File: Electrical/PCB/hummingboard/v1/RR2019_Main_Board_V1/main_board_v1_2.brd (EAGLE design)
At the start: 100 x 75 mm, 144 parts, among them CN1 MIRCO_B, IC1 OR_SC70-5, J10 I2C_5V_4, J11 SERVO_LEFT, J12 SERVO_RIGHT, J13 ESC, J14 5V_INPUT, J15 QUAD_ENCODER_2, J16 7.2V_INPUT, J17 I2C_5V_FXIO_1, J18 I2C_5V_FXIO_2, J19 JETSON_TRIGGER, J2 REAR_ENCODER, J20 QUAD_ENCODER_1, J21 BLDC_HALL, J22 SPI_FXIO_1, J3 FRONT_ENCODER, J4 I2C_1V8_1, J5 SPI_2, J6 WIRELESS_MODULE, J7 UART_0, J8 UART_2, J9 STEERING_ANGLE, Q1 BSS138, Q3 DMP2066LSN, Q4 BSS138, Q5 BSS138, Q6 BSS138, Q7 BSS138, Q8 BSS138, U3 ICM-20948, U4 PCA9306

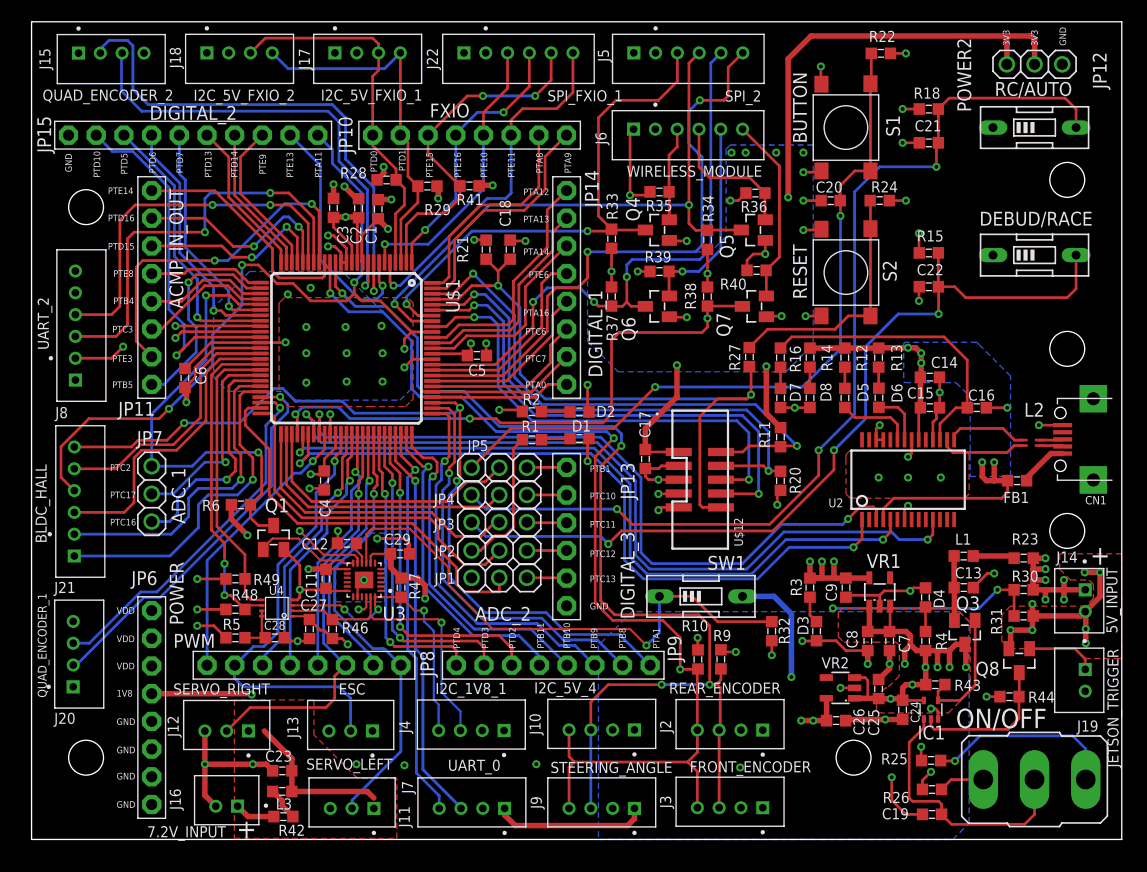
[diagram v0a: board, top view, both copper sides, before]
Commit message: increase 7.2V power plane size
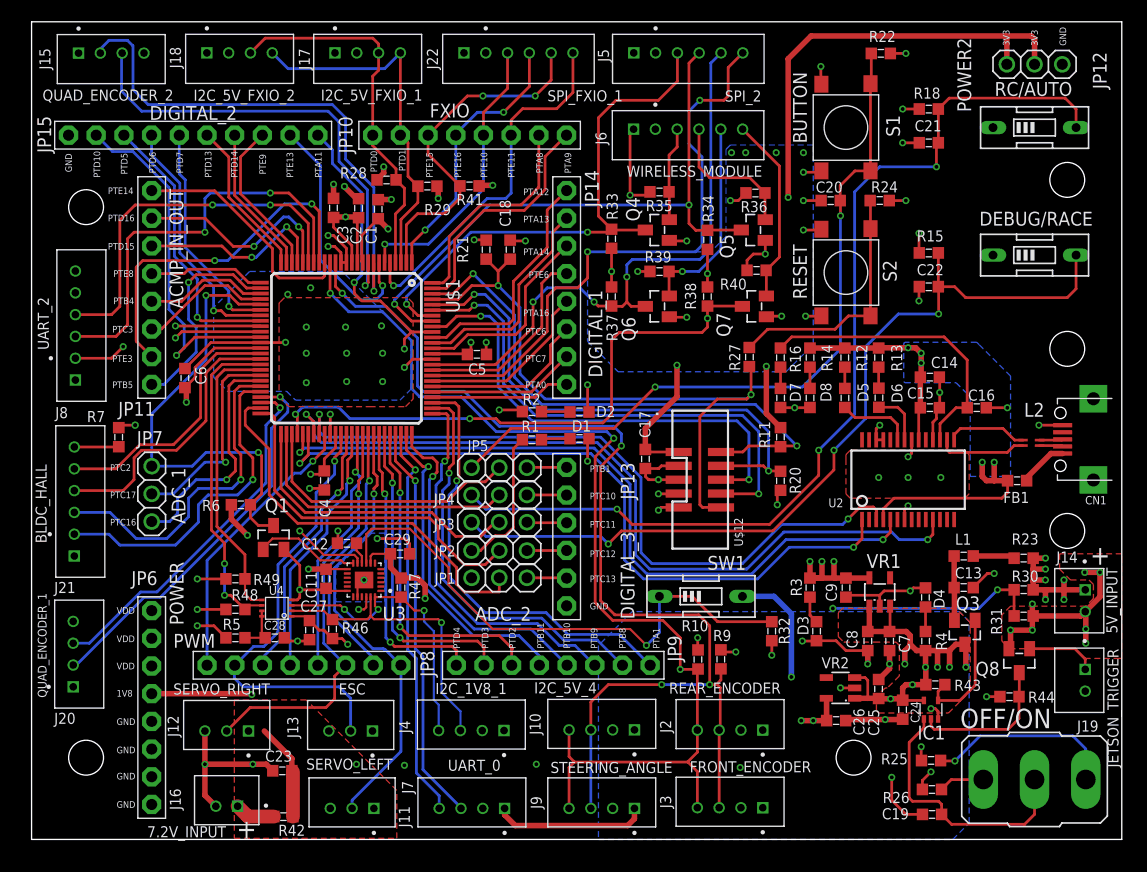
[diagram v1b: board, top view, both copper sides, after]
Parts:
- removed L3: TBD, RobotRacing2019_Master:0603SMT
- added R7: TBD, RobotRacing2019_Master:0603SMT
- S3: value ON/OFF -> OFF/ON
- moved C27 0.10 mm to (25.5, 19.2)
- moved C5 0.10 mm to (40.9, 44.5)
- renumbered DEBUD/RACE to DEBUG/RACE
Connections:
- removed net N$36: L3.1, R42.1
- new net N$4: J21.6, R7.1
- net +7.2V: now also R42.1; no longer L3.2
- net +VDD: now also R7.2
- net ADC0_SE1_/_ACMP0_IN1_/_FTM1_CH1: no longer J21.6
- net FTM1_CH2_/_ADC0_SE12: now also J21.2; no longer J21.1
- net FTM1_CH3_/_ADC0_SE13: now also J21.3; no longer J21.2
- net FTM1_CH6_/_ADC0_SE8: now also J21.4; no longer J21.3
- net GND: now also J21.1
- net PTA11_/_FTM1_CH5: no longer J21.4
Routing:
- net PTA11_/_FTM1_CH5: track 70.7 -> 26.9 mm, vias 4 -> 2
- net ADC0_SE1_/_ACMP0_IN1_/_FTM1_CH1: track 79.2 -> 40.4 mm, vias 3 -> 1
- net +7.2V: track 14.4 -> 8.80 mm
- net N$4: track 0.00 -> 4.09 mm
- net N$36: track 3.07 -> 0.00 mm
- net FTM1_CH6_/_ADC0_SE8: track 27.9 -> 25.8 mm
- net +VDD: track 153.9 -> 155.5 mm, vias 35 -> 36
- net FTM1_CH3_/_ADC0_SE13: track 29.3 -> 30.5 mm

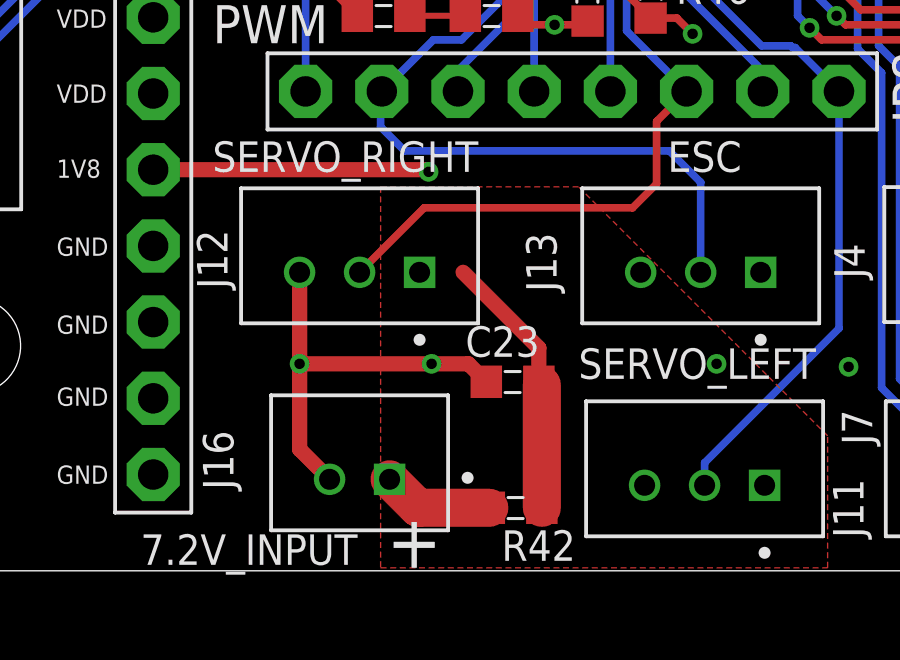
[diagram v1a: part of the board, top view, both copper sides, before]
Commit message: remove inductor from 7.2V input / modify GND plane
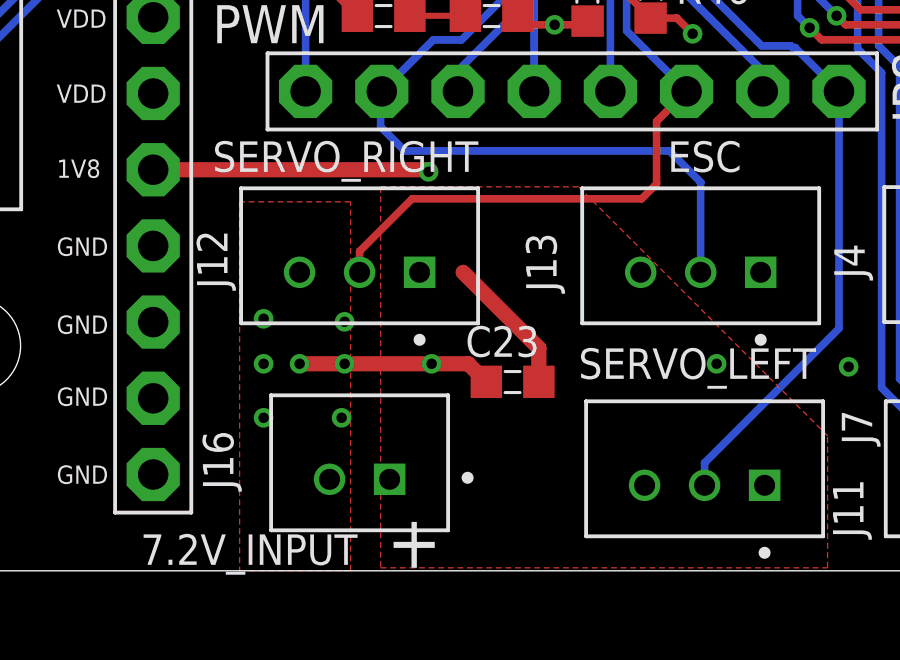
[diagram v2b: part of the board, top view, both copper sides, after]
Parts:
- removed R42: TBD, RobotRacing2019_Master:0603SMT
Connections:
- removed net N$34: J16.1, R42.2
- net +7.2V: now also J16.1; no longer R42.1
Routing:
- net GND: track 178.8 -> 171.5 mm, vias 74 -> 80
- net +7.2V: track 8.80 -> 4.70 mm
- net N$34: track 3.72 -> 0.00 mm
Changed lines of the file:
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@@
 <drawing>
 <settings>
-<setting alwaysvectorfont="yes"/>
+<setting alwaysvectorfont="no"/>
 <setting verticaltext="up"/>
 </settings>
@@
 <attribute name="NAME" x="23.9" y="8.15" size="1.016" layer="25" rot="R180"/>
 </element>
-<element name="R42" library="RobotRacing2019_Master" package="0603SMT" value="TBD" x="23.1" y="2.1" smashed="yes" rot="R180">
-<attribute name="NAME" x="25.1" y="1.35" size="1.016" layer="25" rot="R180"/>
-</element>
 <element name="J19" library="RobotRacing2019_Master" package="JST_B2B-PH-K-S(LF)(SN)" value="JETSON_TRIGGER" x="96.1" y="14.6" smashed="yes" rot="R90">
 <attribute name="NAME" x="95.89608125" y="9.89518125" size="1.01753125" layer="25"/>
@@
 <via x="20.3" y="6.9" extent="1-16" drill="0.35"/>
 <via x="15.9" y="6.9" extent="1-16" drill="0.35"/>
-<wire x1="15.9" y1="6.9" x2="15.9" y2="9.95" width="0.508" layer="1"/>
-<wire x1="16.9" y1="3.05" x2="15.9" y2="4.05" width="0.508" layer="1"/>
-<wire x1="15.9" y1="4.05" x2="15.9" y2="6.9" width="0.508" layer="1"/>
 <wire x1="15.9" y1="6.9" x2="20.3" y2="6.9" width="0.508" layer="1"/>
 <wire x1="20.3" y1="6.9" x2="21.525" y2="6.9" width="0.508" layer="1"/>
@@
 </polygon>
 <contactref element="J21" pad="1"/>
+<via x="14.7" y="6.9" extent="1-16" drill="0.35"/>
+<via x="17.4" y="8.3" extent="1-16" drill="0.35"/>
+<via x="17.4" y="6.9" extent="1-16" drill="0.35"/>
+<via x="17.3" y="5.1" extent="1-16" drill="0.35"/>
+<via x="14.7" y="8.4" extent="1-16" drill="0.35"/>
+<via x="14.7" y="5.1" extent="1-16" drill="0.35"/>
+<polygon width="0.4064" layer="1">
+<vertex x="13.9" y="12.3"/>
+<vertex x="13.9" y="0"/>
+<vertex x="17.4" y="0"/>
+<vertex x="17.6" y="0"/>
+<vertex x="17.6" y="12.2"/>
+<vertex x="17.6" y="12.3"/>
+</polygon>
 </signal>
 <signal name="+VDD">
@@
 <contactref element="J12" pad="2"/>
 <contactref element="JP8" pad="3"/>
-<wire x1="17.9" y1="9.95" x2="20.05" y2="12.1" width="0.254" layer="1"/>
+<wire x1="19.65" y1="12.4" x2="17.9" y2="10.65" width="0.254" layer="1"/>
+<wire x1="17.9" y1="9.95" x2="17.9" y2="10.65" width="0.254" layer="1"/>
 <wire x1="27.8" y1="14.98" x2="28.8" y2="15.98" width="0.254" layer="1"/>
 <wire x1="27.8" y1="14.98" x2="27.8" y2="12.9" width="0.254" layer="1"/>
-<wire x1="20.05" y1="12.1" x2="27" y2="12.1" width="0.254" layer="1"/>
-<wire x1="27" y1="12.1" x2="27.8" y2="12.9" width="0.254" layer="1"/>
+<wire x1="19.65" y1="12.4" x2="27.3" y2="12.4" width="0.254" layer="1"/>
+<wire x1="27.3" y1="12.4" x2="27.8" y2="12.9" width="0.254" layer="1"/>
 <via x="30" y="31.7" extent="1-16" drill="0.35"/>
 <wire x1="30" y1="31.7" x2="30" y2="28.6" width="0.254" layer="16"/>
@@
 <contactref element="J11" pad="1"/>
 <contactref element="J12" pad="1"/>
-<polygon width="0.508" layer="1" rank="2">
+<polygon width="0.8128" layer="1" rank="2">
 <vertex x="18.6" y="12.8"/>
 <vertex x="18.6" y="0.1"/>
@@
 <vertex x="25.2" y="12.8"/>
 </polygon>
-<contactref element="R42" pad="1"/>
-<wire x1="23.975" y1="2.1" x2="23.975" y2="6.2" width="1.27" layer="1"/>
-</signal>
-<signal name="N$34">
 <contactref element="J16" pad="1"/>
-<contactref element="R42" pad="2"/>
-<wire x1="18.9" y1="3.05" x2="19.85" y2="2.1" width="1.27" layer="1"/>
-<wire x1="19.85" y1="2.1" x2="22.225" y2="2.1" width="1.27" layer="1"/>
 </signal>
 <signal name="N$39">

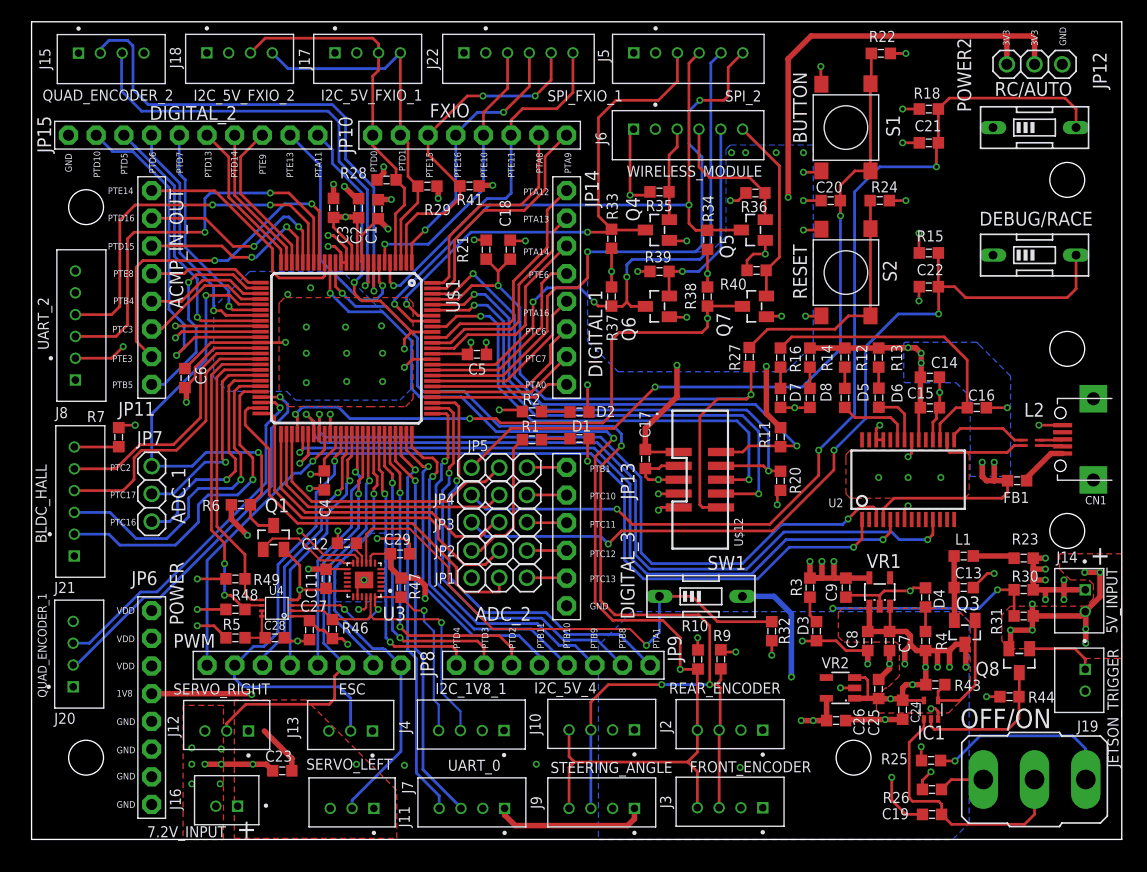
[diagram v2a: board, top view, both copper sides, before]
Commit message: add extra GND plane and via
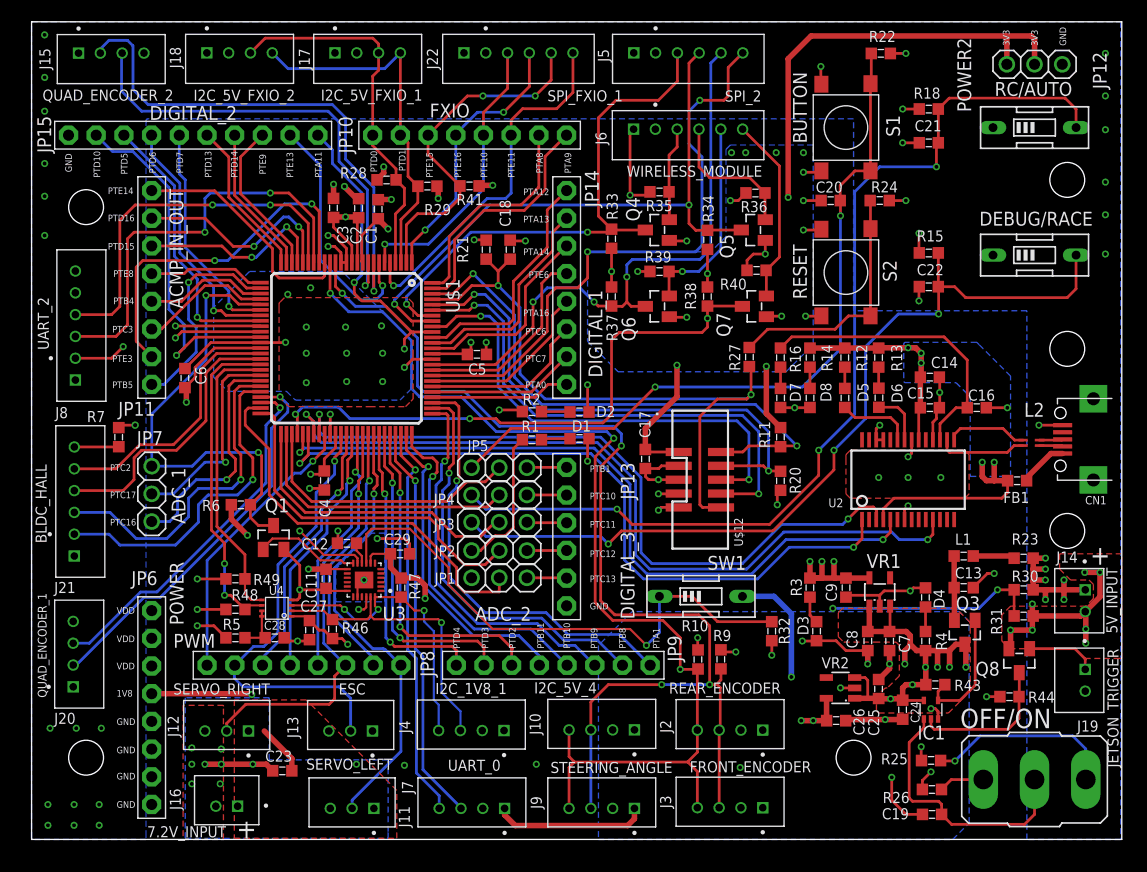
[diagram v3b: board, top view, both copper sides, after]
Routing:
- net GND: vias 80 -> 101
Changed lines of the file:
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@@
 <drawing>
 <settings>
-<setting alwaysvectorfont="no"/>
+<setting alwaysvectorfont="yes"/>
 <setting verticaltext="up"/>
 </settings>
@@
 <vertex x="100" y="75"/>
 </polygon>
-<polygon width="0.254" layer="2">
+<polygon width="0.508" layer="2">
 <vertex x="14.1" y="0.1"/>
 <vertex x="14.1" y="12.9"/>
@@
 <vertex x="17.6" y="12.3"/>
 </polygon>
+<polygon width="0.508" layer="16">
+<vertex x="14.1" y="13"/>
+<vertex x="14.1" y="0.1"/>
+<vertex x="32.7" y="0.1"/>
+<vertex x="32.7" y="0.7"/>
+<vertex x="32.7" y="7.3"/>
+<vertex x="21.8" y="7.3"/>
+<vertex x="21.8" y="13"/>
+</polygon>
+<polygon width="0.254" layer="16">
+<vertex x="0" y="75"/>
+<vertex x="99.9" y="75"/>
+<vertex x="99.9" y="0"/>
+<vertex x="91.3" y="0"/>
+<vertex x="91.3" y="46.6"/>
+<vertex x="91.3" y="48.5"/>
+<vertex x="75.4" y="48.5"/>
+<vertex x="75.4" y="66.1"/>
+<vertex x="65.4" y="66.1"/>
+<vertex x="60.6" y="66.1"/>
+<vertex x="15.2" y="66.1"/>
+<vertex x="10.6" y="66.1"/>
+<vertex x="10.5" y="66"/>
+<vertex x="10.5" y="0.7"/>
+<vertex x="10.5" y="0"/>
+<vertex x="0.1" y="0"/>
+<vertex x="0" y="0.1"/>
+</polygon>
+<via x="1.2" y="73.8" extent="1-16" drill="0.35"/>
+<via x="1.2" y="69.9" extent="1-16" drill="0.35"/>
+<via x="1.5" y="1.3" extent="1-16" drill="0.35"/>
+<via x="3.9" y="1.3" extent="1-16" drill="0.35"/>
+<via x="6.2" y="1.3" extent="1-16" drill="0.35"/>
+<via x="1.5" y="3.2" extent="1-16" drill="0.35"/>
+<via x="3.9" y="3.2" extent="1-16" drill="0.35"/>
+<via x="6.2" y="3.2" extent="1-16" drill="0.35"/>
+<via x="1.7" y="10.2" extent="1-16" drill="0.35"/>
+<via x="4.1" y="10.2" extent="1-16" drill="0.35"/>
+<via x="6.4" y="10.2" extent="1-16" drill="0.35"/>
+<via x="1.2" y="66.8" extent="1-16" drill="0.35"/>
+<via x="1.2" y="62" extent="1-16" drill="0.35"/>
+<via x="1.2" y="59" extent="1-16" drill="0.35"/>
+<via x="1.2" y="55.4" extent="1-16" drill="0.35"/>
+<via x="98.5" y="72.1" extent="1-16" drill="0.35"/>
+<via x="98.5" y="68.2" extent="1-16" drill="0.35"/>
+<via x="98.5" y="65.1" extent="1-16" drill="0.35"/>
+<via x="98.5" y="60.3" extent="1-16" drill="0.35"/>
+<via x="98.5" y="57.3" extent="1-16" drill="0.35"/>
+<via x="98.5" y="53.7" extent="1-16" drill="0.35"/>
 </signal>
 <signal name="+VDD">

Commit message: add filter values
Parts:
- C13: value TBD -> 100ohm
- L1: value TBD -> 4.7u
- R23: value TBD -> 0
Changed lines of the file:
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@@
 <drawing>
 <settings>
-<setting alwaysvectorfont="yes"/>
+<setting alwaysvectorfont="no"/>
 <setting verticaltext="up"/>
 </settings>
@@
 <layers>
 <layer number="1" name="Top" color="4" fill="1" visible="yes" active="yes"/>
-<layer number="2" name="GND" color="16" fill="3" visible="yes" active="yes"/>
+<layer number="2" name="GND" color="16" fill="3" visible="no" active="yes"/>
 <layer number="3" name="Route3" color="17" fill="1" visible="no" active="no"/>
 <layer number="4" name="Route4" color="18" fill="1" visible="no" active="no"/>
@@
 <layer number="13" name="Route13" color="21" fill="1" visible="no" active="no"/>
 <layer number="14" name="Route14" color="22" fill="1" visible="no" active="no"/>
-<layer number="15" name="POWER" color="23" fill="6" visible="yes" active="yes"/>
-<layer number="16" name="Bottom" color="1" fill="1" visible="yes" active="yes"/>
-<layer number="17" name="Pads" color="2" fill="1" visible="yes" active="yes"/>
+<layer number="15" name="POWER" color="23" fill="6" visible="no" active="yes"/>
+<layer number="16" name="Bottom" color="1" fill="1" visible="no" active="yes"/>
+<layer number="17" name="Pads" color="2" fill="1" visible="no" active="yes"/>
 <layer number="18" name="Vias" color="2" fill="1" visible="yes" active="yes"/>
 <layer number="19" name="Unrouted" color="6" fill="1" visible="yes" active="yes"/>
@@
 <attribute name="NAME" x="87.005" y="22.295" size="1.27" layer="25" rot="R180"/>
 </element>
-<element name="C13" library="RobotRacing2019_Master" package="0603SMT" value="TBD" x="85.5" y="23.1" smashed="yes">
+<element name="C13" library="RobotRacing2019_Master" package="0603SMT" value="100ohm" x="85.5" y="23.1" smashed="yes">
 <attribute name="NAME" x="84.7" y="23.95" size="1.016" layer="25"/>
 </element>
-<element name="L1" library="RobotRacing2019_Master" package="0603SMT" value="TBD" x="85.5" y="26" smashed="yes" rot="R180">
+<element name="L1" library="RobotRacing2019_Master" package="0603SMT" value="4.7u" x="85.5" y="26" smashed="yes" rot="R180">
 <attribute name="NAME" x="86.2" y="28.05" size="1.016" layer="25" rot="R180"/>
 </element>
@@
 <attribute name="VALUE" x="99.601509375" y="18.89861875" size="1.01643125" layer="21" rot="R90"/>
 </element>
-<element name="R23" library="RobotRacing2019_Master" package="0603SMT" value="TBD" x="91" y="25.8" smashed="yes">
+<element name="R23" library="RobotRacing2019_Master" package="0603SMT" value="0" x="91" y="25.8" smashed="yes">
 <attribute name="NAME" x="89.9" y="27.05" size="1.016" layer="25"/>
 </element>
